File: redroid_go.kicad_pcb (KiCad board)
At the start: 2 copper layers, 70 x 95 mm, 99 parts, among them J1 USB4105-GF-A, J2 5051101892, J3 Conn_01x02_Pin, J4 Conn_01x10_Pin, Q1 UMH3N, Q2 PMOS, Q3 UMH3N, SW1 UP, SW10 A, SW11 SW_SPDT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

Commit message: Minor fixes in PCB
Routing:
- net RESET: track 89.7 -> 89.0 mm
- net IO26: track 97.2 -> 96.5 mm
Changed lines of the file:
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@@
 	)
 	(gr_rect
-		(start 130.5 57.14)
-		(end 190.76 99.86)
+		(start 133.5 55)
+		(end 193.76 97.72)
 		(stroke
 			(width 0.1)
@@
 	)
 	(segment
-		(start 170.5 67)
-		(end 170.5 65.5)
-		(width 0.2)
-		(layer "F.Cu")
-		(net 6)
-	)
-	(segment
-		(start 165.25 60.25)
-		(end 165 60.25)
-		(width 0.2)
-		(layer "F.Cu")
-		(net 6)
-	)
-	(segment
-		(start 170.5 65.5)
-		(end 165.25 60.25)
+		(start 170.5 66.75)
+		(end 164 60.25)
 		(width 0.2)
 		(layer "F.Cu")
@@
 	)
 	(via
-		(at 165 60.25)
+		(at 164 60.25)
 		(size 0.6)
 		(drill 0.3)
@@
 	)
 	(via
-		(at 170.5 67)
+		(at 170.5 66.75)
 		(size 0.6)
 		(drill 0.3)
@@
 		(drill 0.3)
 		(layers "F.Cu" "B.Cu")
-		(net 6)
-	)
-	(segment
-		(start 171.25 76.25)
-		(end 170.5 75.5)
-		(width 0.2)
-		(layer "B.Cu")
 		(net 6)
 	)
@@
 	)
 	(segment
+		(start 170.5 66.75)
+		(end 170.5 75.5)
+		(width 0.2)
+		(layer "B.Cu")
+		(net 6)
+	)
+	(segment
 		(start 170.375 69.625)
 		(end 167.375 69.625)
@@
 	)
 	(segment
+		(start 195.45 62.7)
+		(end 195.45 60.25)
+		(width 0.2)
+		(layer "B.Cu")
+		(net 6)
+	)
+	(segment
+		(start 164 60.25)
+		(end 162.75 60.25)
+		(width 0.2)
+		(layer "B.Cu")
+		(net 6)
+	)
+	(segment
+		(start 193.4493 54.54)
+		(end 195.4875 56.5782)
+		(width 0.2)
+		(layer "B.Cu")
+		(net 6)
+	)
+	(segment
+		(start 192.5 54.54)
+		(end 182.71 54.54)
+		(width 0.2)
+		(layer "B.Cu")
+		(net 6)
+	)
+	(segment
+		(start 170.5 75.5)
+		(end 171.25 76.25)
+		(width 0.2)
+		(layer "B.Cu")
+		(net 6)
+	)
+	(segment
+		(start 163.85 73.15)
+		(end 157 73.15)
+		(width 0.2)
+		(layer "B.Cu")
+		(net 6)
+	)
+	(segment
+		(start 178.75 76)
+		(end 178.5 76.25)
+		(width 0.2)
+		(layer "B.Cu")
+		(net 6)
+	)
+	(segment
+		(start 195.4875 56.5782)
+		(end 195.4875 60.2)
+		(width 0.2)
+		(layer "B.Cu")
+		(net 6)
+	)
+	(segment
 		(start 162.75 60.25)
 		(end 161.35 61.65)
@@
 	)
 	(segment
-		(start 195.45 62.7)
-		(end 195.45 60.25)
-		(width 0.2)
-		(layer "B.Cu")
-		(net 6)
-	)
-	(segment
-		(start 193.4493 54.54)
-		(end 195.4875 56.5782)
-		(width 0.2)
-		(layer "B.Cu")
-		(net 6)
-	)
-	(segment
-		(start 192.5 54.54)
-		(end 182.71 54.54)
-		(width 0.2)
-		(layer "B.Cu")
-		(net 6)
-	)
-	(segment
-		(start 163.85 73.15)
-		(end 157 73.15)
-		(width 0.2)
-		(layer "B.Cu")
-		(net 6)
-	)
-	(segment
 		(start 161.35 61.65)
 		(end 159.83 61.65)
@@
 	)
 	(segment
-		(start 178.75 76)
-		(end 178.5 76.25)
-		(width 0.2)
-		(layer "B.Cu")
-		(net 6)
-	)
-	(segment
-		(start 195.4875 56.5782)
-		(end 195.4875 60.2)
-		(width 0.2)
-		(layer "B.Cu")
-		(net 6)
-	)
-	(segment
-		(start 165 60.25)
-		(end 162.75 60.25)
-		(width 0.2)
-		(layer "B.Cu")
-		(net 6)
-	)
-	(segment
-		(start 170.5 75.5)
-		(end 170.5 67)
-		(width 0.2)
-		(layer "B.Cu")
-		(net 6)
-	)
-	(segment
 		(start 178.75 58.5)
 		(end 178.75 76)
@@
 	)
 	(segment
+		(start 180.5 76.5)
+		(end 180.5 69.5)
+		(width 0.2)
+		(layer "F.Cu")
+		(net 10)
+	)
+	(segment
+		(start 134 114)
+		(end 138.545 109.455)
+		(width 0.2)
+		(layer "F.Cu")
+		(net 10)
+	)
+	(segment
+		(start 138.545 109.455)
+		(end 156.545 109.455)
+		(width 0.2)
+		(layer "F.Cu")
+		(net 10)
+	)
+	(segment
+		(start 161.5 95.5)
+		(end 175 82)
+		(width 0.2)
+		(layer "F.Cu")
+		(net 10)
+	)
+	(segment
+		(start 175 82)
+		(end 180.5 76.5)
+		(width 0.2)
+		(layer "F.Cu")
+		(net 10)
+	)
+	(segment
+		(start 174.9 82.1)
+		(end 175 82)
+		(width 0.2)
+		(layer "F.Cu")
+		(net 10)
+	)
+	(segment
+		(start 134 115)
+		(end 134 114)
+		(width 0.2)
+		(layer "F.Cu")
+		(net 10)
+	)
+	(segment
 		(start 180.5 69.5)
 		(end 181.5 68.5)
@@
 	)
 	(segment
-		(start 175.485785 82.1)
-		(end 176.9 82.1)
-		(width 0.2)
-		(layer "F.Cu")
-		(net 10)
-	)
-	(segment
-		(start 161.5 104.5)
-		(end 161.5 96.085785)
-		(width 0.2)
-		(layer "F.Cu")
-		(net 10)
-	)
-	(segment
-		(start 134 115)
-		(end 134 114)
-		(width 0.2)
-		(layer "F.Cu")
-		(net 10)
-	)
-	(segment
-		(start 180.5 78.5)
-		(end 180.5 69.5)
-		(width 0.2)
-		(layer "F.Cu")
-		(net 10)
-	)
-	(segment
-		(start 176.9 82.1)
-		(end 180.5 78.5)
-		(width 0.2)
-		(layer "F.Cu")
-		(net 10)
-	)
-	(segment
 		(start 156.545 109.455)
 		(end 161.5 104.5)
@@
 	)
 	(segment
-		(start 134 114)
-		(end 138.545 109.455)
-		(width 0.2)
-		(layer "F.Cu")
-		(net 10)
-	)
-	(segment
-		(start 161.5 96.085785)
-		(end 175.485785 82.1)
-		(width 0.2)
-		(layer "F.Cu")
-		(net 10)
-	)
-	(segment
-		(start 138.545 109.455)
-		(end 156.545 109.455)
+		(start 161.5 104.5)
+		(end 161.5 95.5)
 		(width 0.2)
 		(layer "F.Cu")
@@
 	)
 	(segment
-		(start 171.934314 61.5)
-		(end 172 61.5)
+		(start 155.6 73.565686)
+		(end 155.6 72.134312)
 		(width 0.2)
 		(layer "B.Cu")
@@
 	)
 	(segment
-		(start 172 60.4007)
+		(start 156.95 74.099998)
+		(end 156.134312 74.099998)
+		(width 0.2)
+		(layer "B.Cu")
+		(net 32)
+	)
+	(segment
+		(start 155.6 72.134312)
+		(end 158.734312 69)
+		(width 0.2)
+		(layer "B.Cu")
+		(net 32)
+	)
+	(segment
+		(start 172.136901 61.297413)
+		(end 172.136901 60.263799)
+		(width 0.2)
+		(layer "B.Cu")
+		(net 32)
+	)
+	(segment
+		(start 164.434314 69)
+		(end 172.136901 61.297413)
+		(width 0.2)
+		(layer "B.Cu")
+		(net 32)
+	)
+	(segment
+		(start 172.136901 60.263799)
 		(end 174.0507 58.35)
 		(width 0.2)
@@
 	)
 	(segment
-		(start 164.434314 69)
-		(end 171.934314 61.5)
+		(start 174.0507 58.35)
+		(end 175 58.35)
 		(width 0.2)
 		(layer "B.Cu")
@@
 	)
 	(segment
-		(start 172 61.5)
-		(end 172 60.4007)
-		(width 0.2)
-		(layer "B.Cu")
-		(net 32)
-	)
-	(segment
 		(start 156.134312 74.099998)
 		(end 155.6 73.565686)
 		(width 0.2)
 		(layer "B.Cu")
-		(net 32)
-	)
-	(segment
-		(start 155.6 73.565686)
-		(end 155.6 72.134312)
-		(width 0.2)
-		(layer "B.Cu")
-		(net 32)
-	)
-	(segment
-		(start 174.0507 58.35)
-		(end 175 58.35)
-		(width 0.2)
-		(layer "B.Cu")
-		(net 32)
-	)
-	(segment
-		(start 156.95 74.099998)
-		(end 156.134312 74.099998)
-		(width 0.2)
-		(layer "B.Cu")
-		(net 32)
-	)
-	(segment
-		(start 155.6 72.134312)
-		(end 158.734312 69)
-		(width 0.2)
-		(layer "B.Cu")

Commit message: Minor fixes in PCB
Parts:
- moved R16 0.75 mm to (176.5, 78.5)
- moved C14 0.36 mm to (133.0, 131.5)
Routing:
- net GND: track 75.2 -> 76.0 mm
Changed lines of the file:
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@@
 	(footprint "Capacitor_SMD:C_0603_1608Metric_Pad1.08x0.95mm_HandSolder"
 		(layer "B.Cu")
-		(at 133 131.1375 90)
+		(at 133 131.5 90)
 		(descr "Capacitor SMD 0603 (1608 Metric), square (rectangular) end terminal, IPC_7351 nominal with elongated pad for handsoldering. (Body size source: IPC-SM-782 page 76, https://www.pcb-3d.com/wordpress/wp-content/uploads/ipc-sm-782a_amendment_1_and_2.pdf), generated with kicad-footprint-generator")
 		(tags "capacitor handsolder")
@@
 		(tags "capacitor handsolder")
 		(property "Reference" "C13"
-			(at 1.8625 1.5 0)
+			(at -0.1375 1.5 0)
 			(layer "B.SilkS")
 			(effects
@@
 		(tags "capacitor handsolder")
 		(property "Reference" "C16"
-			(at 0 1.43 0)
+			(at 0 -1.5 0)
 			(layer "B.SilkS")
 			(effects
@@
 	(footprint "Resistor_SMD:R_0603_1608Metric_Pad0.98x0.95mm_HandSolder"
 		(layer "B.Cu")
-		(at 176.5 77.75)
+		(at 176.5 78.5)
 		(descr "Resistor SMD 0603 (1608 Metric), square (rectangular) end terminal, IPC_7351 nominal with elongated pad for handsoldering. (Body size source: IPC-SM-782 page 72, https://www.pcb-3d.com/wordpress/wp-content/uploads/ipc-sm-782a_amendment_1_and_2.pdf), generated with kicad-footprint-generator")
 		(tags "resistor handsolder")
 		(property "Reference" "R16"
-			(at 0 1.43 0)
+			(at 0 2 0)
 			(layer "B.SilkS")
 			(effects
@@
 	)
 	(via
-		(at 133.5 109)
+		(at 134.5 110)
 		(size 0.6)
 		(drill 0.3)
@@
 	)
 	(segment
-		(start 141.75 114.75)
-		(end 141.5 115)
-		(width 0.2)
-		(layer "B.Cu")
-		(net 1)
-	)
-	(segment
 		(start 160.029999 55.05)
 		(end 159.25 55.05)
@@
 	)
 	(segment
-		(start 141.5 118.8)
-		(end 141.95 119.25)
-		(width 0.2)
-		(layer "B.Cu")
-		(net 1)
-	)
-	(segment
 		(start 167.057201 99.66545)
 		(end 165.77795 99.66545)
@@
 	)
 	(segment
+		(start 141 114.880026)
+		(end 141 118.3)
+		(width 0.2)
+		(layer "B.Cu")
+		(net 1)
+	)
+	(segment
 		(start 154 123.5)
 		(end 151.31585 123.5)
@@
 	)
 	(segment
+		(start 141.130026 114.75)
+		(end 141 114.880026)
+		(width 0.2)
+		(layer "B.Cu")
+		(net 1)
+	)
+	(segment
 		(start 157.5 56)
 		(end 155.5 56)
@@
 	)
 	(segment
-		(start 141.5 115)
-		(end 141.5 118.8)
-		(width 0.2)
-		(layer "B.Cu")
-		(net 1)
-	)
-	(segment
 		(start 168.5 99.7541)
 		(end 168.5 98.25)
@@
 	)
 	(segment
+		(start 142.95 114.75)
+		(end 141.130026 114.75)
+		(width 0.2)
+		(layer "B.Cu")
+		(net 1)
+	)
+	(segment
 		(start 166.5 56)
 		(end 169.5 56)
@@
 	)
 	(segment
-		(start 142.95 114.75)
-		(end 141.75 114.75)
-		(width 0.2)
-		(layer "B.Cu")
-		(net 1)
-	)
-	(segment
 		(start 168.41135 99.66545)
 		(end 167.057201 99.66545)
@@
 	)
 	(segment
+		(start 141 118.3)
+		(end 141.95 119.25)
+		(width 0.2)
+		(layer "B.Cu")
+		(net 1)
+	)
+	(segment
 		(start 158.400001 76.099999)
 		(end 156.95 76.099999)
@@
 	)
 	(segment
-		(start 173.25 81.25)
-		(end 170.598529 81.25)
+		(start 174.5 80)
+		(end 173.25 81.25)
 		(width 0.2)
 		(layer "F.Cu")
@@
 	)
 	(segment
-		(start 150.848529 101)
-		(end 150.5 101)
+		(start 170.598529 81.25)
+		(end 150.848529 101)
 		(width 0.2)
 		(layer "F.Cu")
@@
 	)
 	(segment
-		(start 149.5 103.48452)
-		(end 149.75774 103.74226)
+		(start 150.848529 101)
+		(end 150.5 101)
 		(width 0.2)
 		(layer "F.Cu")
@@
 	)
 	(segment
-		(start 175.5 79)
-		(end 173.25 81.25)
+		(start 149.5 103.48452)
+		(end 149.75774 103.74226)
 		(width 0.2)
 		(layer "F.Cu")
@@
 	)
 	(segment
-		(start 170.598529 81.25)
-		(end 150.848529 101)
+		(start 173.25 81.25)
+		(end 170.598529 81.25)
 		(width 0.2)
 		(layer "F.Cu")
@@
 	)
 	(via
-		(at 175.5 79)
+		(at 174.5 80)
 		(size 0.6)
 		(drill 0.3)
@@
 	)
 	(segment
-		(start 175.5875 78.9125)
-		(end 175.5 79)
+		(start 157.17 59.85)
+		(end 157.17 60.35)
 		(width 0.2)
 		(layer "B.Cu")
@@
 	)
 	(segment
-		(start 157.17 59.85)
-		(end 157.17 60.35)
+		(start 176.5 75.34853)
+		(end 176.5 69.0607)
 		(width 0.2)
 		(layer "B.Cu")
@@
 	)
 	(segment
-		(start 176.5 75.34853)
-		(end 176.5 69.0607)
+		(start 174.5 80)
+		(end 175.5875 78.9125)
+		(width 0.2)
+		(layer "B.Cu")
+		(net 50)
+	)
+	(segment
+		(start 175.5875 78.9125)
+		(end 175.5875 77.75)
 		(width 0.2)
 		(layer "B.Cu")
@@
 		(width 0.2)
 		(layer "B.Cu")
-		(net 50)
-	)
-	(segment
-		(start 175.5875 77.75)
-		(end 175.5875 78.9125)
-		(width 0.2)
-		(layer "B.Cu")

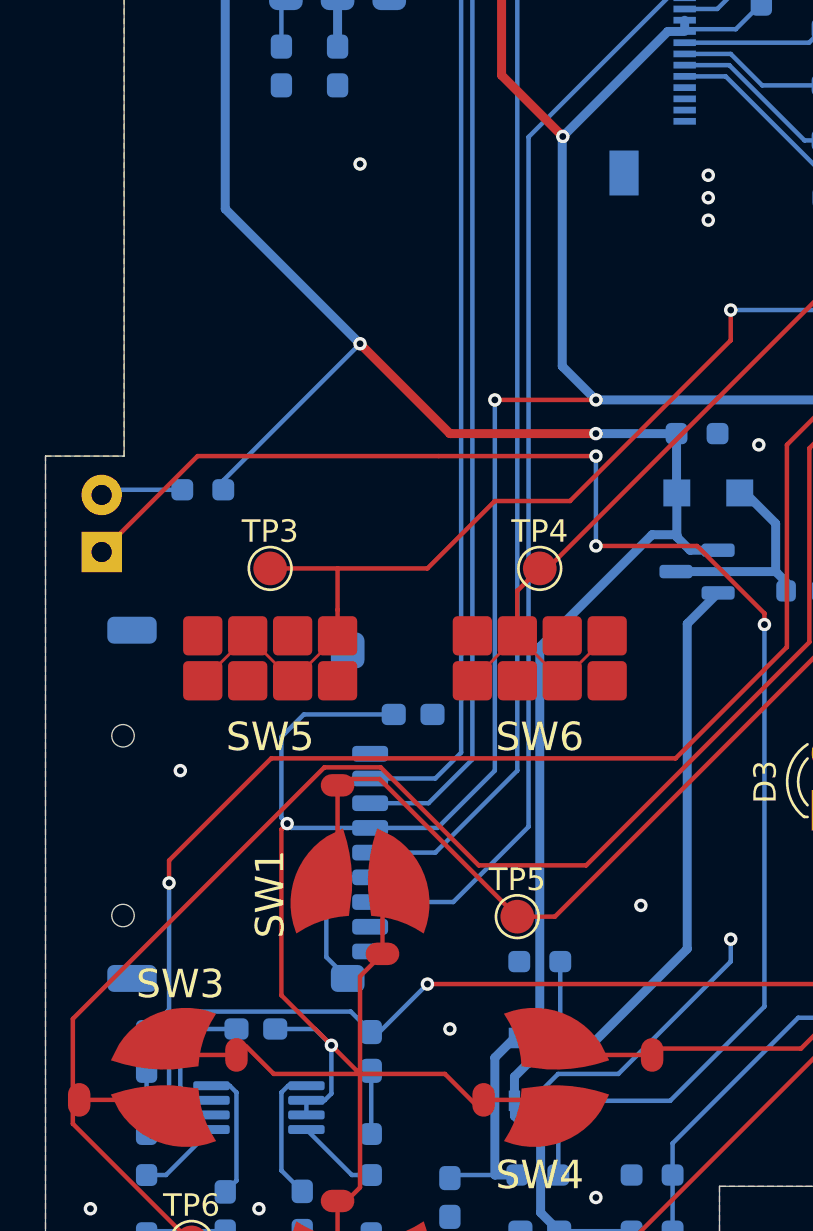
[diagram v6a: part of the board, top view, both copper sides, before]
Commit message: Move SD socket
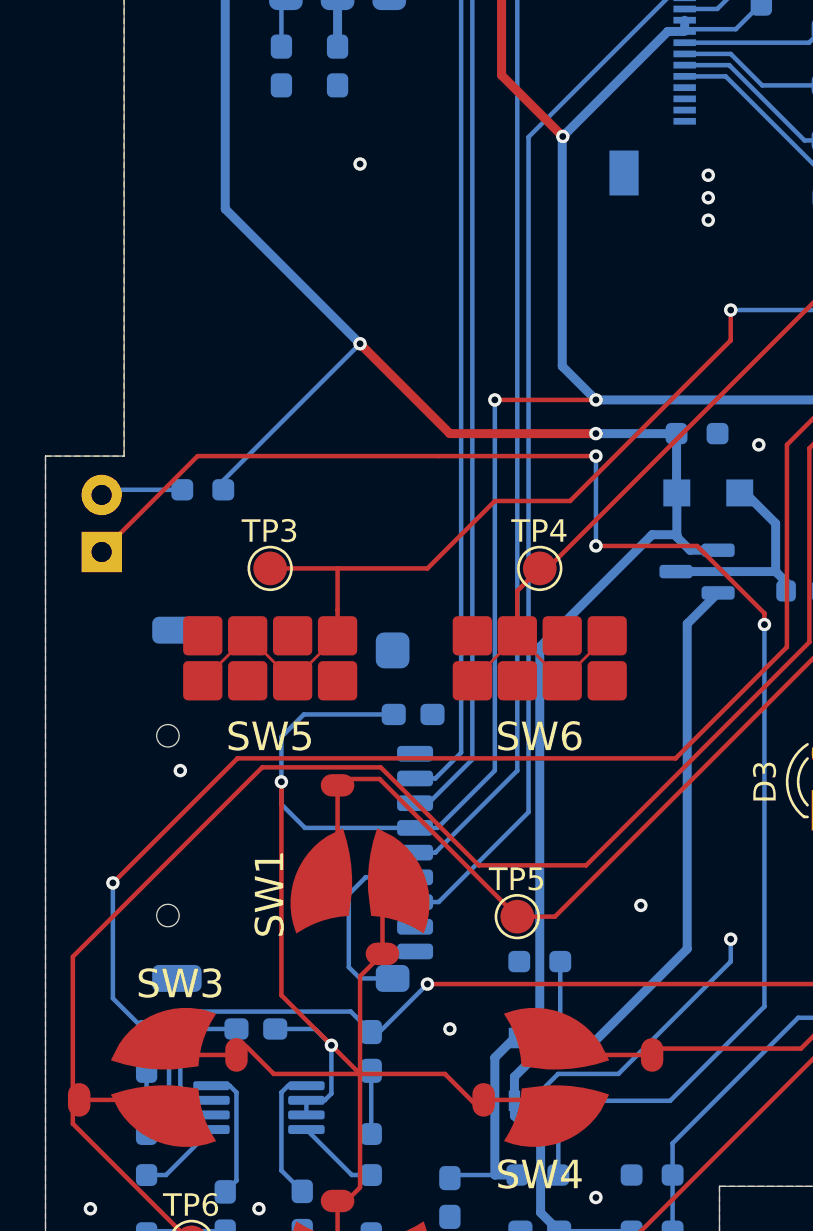
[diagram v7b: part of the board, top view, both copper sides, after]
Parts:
- moved U6 2.00 mm to (138.9, 118.0)
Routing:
- net MOSI: track 95.7 -> 93.1 mm
- net MISO: track 101.4 -> 99.0 mm
- net IO26: track 96.5 -> 98.6 mm
- net SCK: track 95.5 -> 93.5 mm
- net CS1: track 77.8 -> 75.8 mm
- net GND: track 76.0 -> 77.9 mm
- net IO34: track 128.0 -> 129.6 mm
- net P3V3: track 266.7 -> 267.9 mm

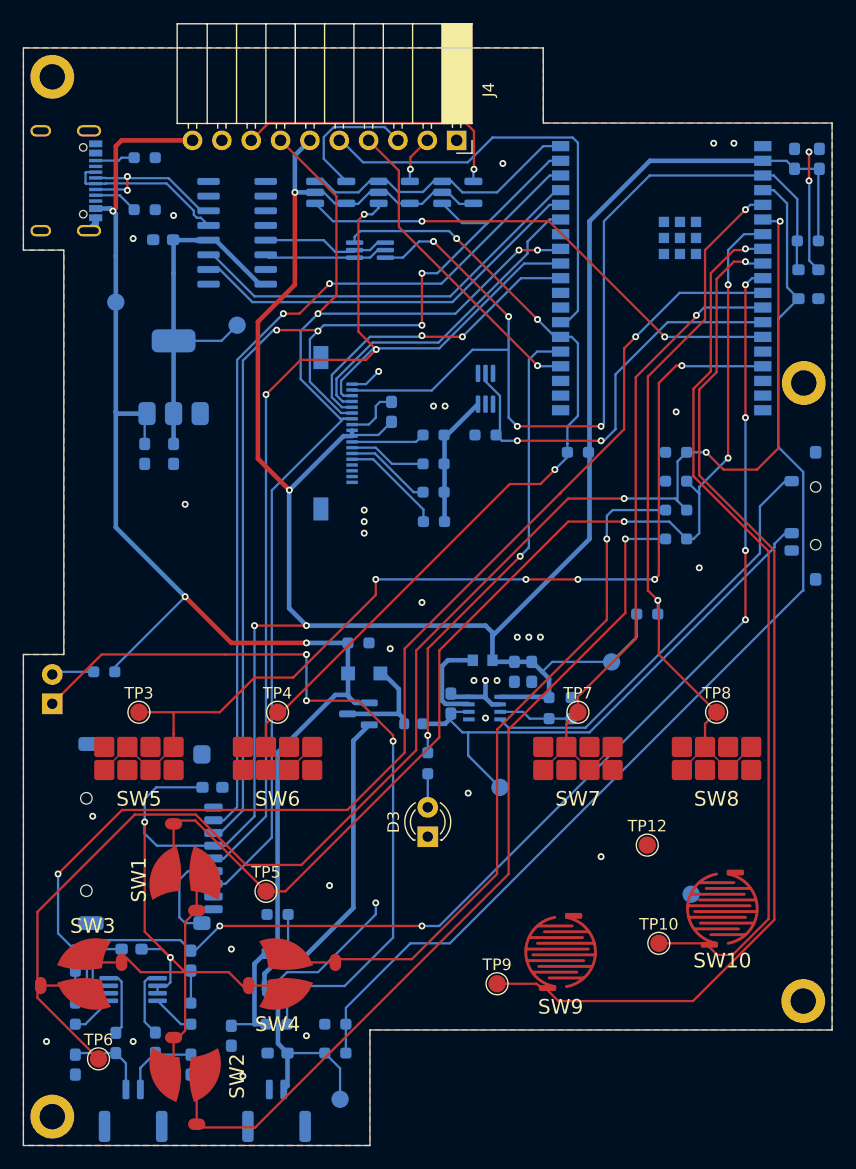
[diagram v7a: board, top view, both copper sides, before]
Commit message: Move display connector and minor fixes
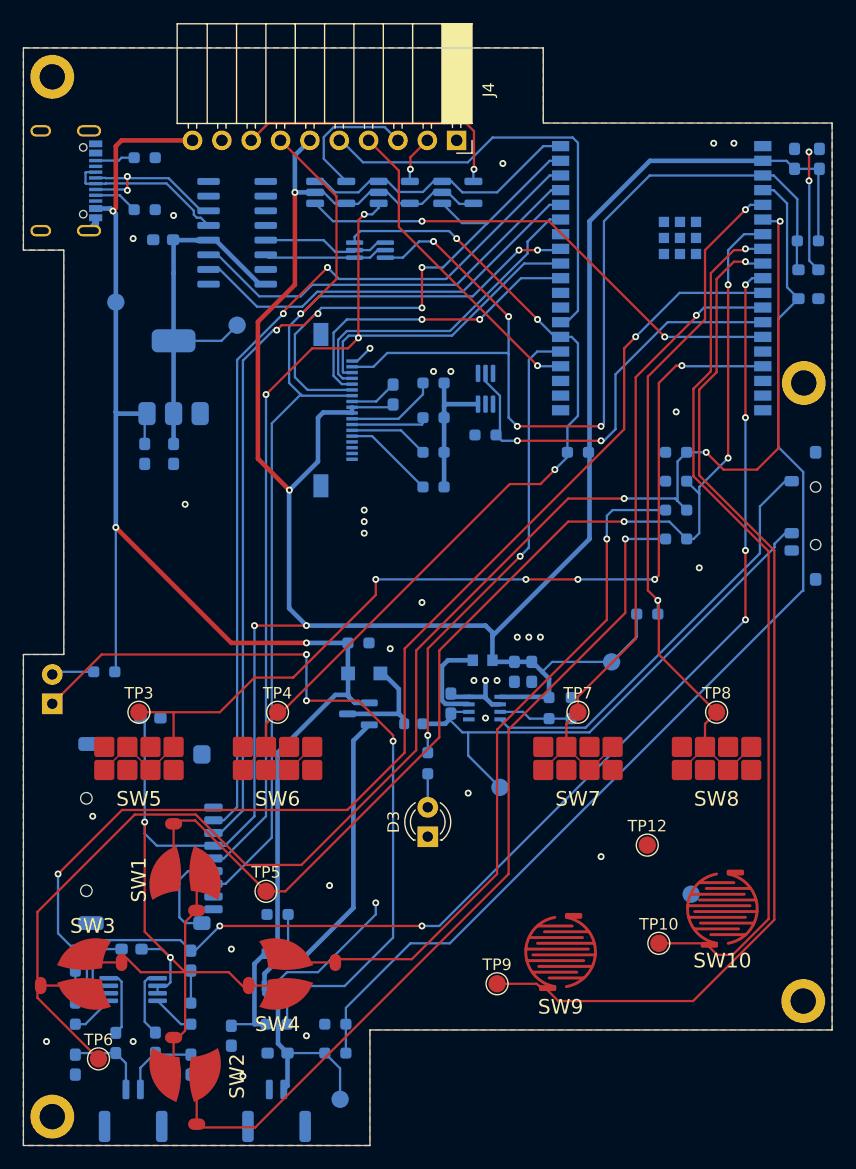
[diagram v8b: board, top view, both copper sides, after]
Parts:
- moved C16 8.05 mm to (139.5, 101.5)
- moved R24 4.50 mm to (164.0, 72.5)
- moved R25 4.00 mm to (164.0, 75.5)
- moved R19 3.45 mm to (164.0, 78.5)
- moved R26 3.00 mm to (164.0, 81.5)
- moved J2 2.00 mm to (154.5, 74.8)
- moved C10 1.51 mm to (160.5, 73.5)
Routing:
- net P3V3: track 267.9 -> 272.6 mm
- net VBUS: track 122.9 -> 126.4 mm
- net SCK: track 93.5 -> 90.5 mm
- net MISO: track 99.0 -> 101.5 mm
- net MOSI: track 93.1 -> 94.9 mm
- net GND: track 77.9 -> 76.5 mm
- net Net-(Q3A-C1): track 11.4 -> 12.5 mm
- net Net-(J2-LEDK1): track 6.39 -> 7.49 mm
- net Net-(J2-LEDK4): track 9.03 -> 7.96 mm
- net CS1: track 75.8 -> 76.8 mm
- net RESET: track 89.0 -> 88.2 mm
- net Net-(J2-LEDK3): track 7.53 -> 6.92 mm
- net Net-(J2-LEDK2): track 6.72 -> 6.18 mm
